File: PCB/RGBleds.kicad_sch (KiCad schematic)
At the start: 17 parts, among them Q21 Q_NPN_BCE, Q22 Q_NPN_BCE, Q23 Q_NPN_BCE

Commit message: made some Changes
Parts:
- removed R22, R24, R26: 1k, Resistor_SMD:R_1206_3216Metric_Pad1.30x1.75mm_HandSolder, symbol Device:R
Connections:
- net LEDG_VCC is gone; now on net VCC: D21.5 (GA), D22.5 (GA), D23.5 (GA), D24.5 (GA), D25.5 (GA), D26.5 (GA), D27.5 (GA), D28.5 (GA)
- net LEDR_VCC is gone; now on net VCC: D21.6 (RA), D22.6 (RA), D23.6 (RA), D24.6 (RA), D25.6 (RA), D26.6 (RA), D27.6 (RA), D28.6 (RA)
- net LEDR: now reaches Q21.1 (B)
- net LEDG: now reaches Q22.1 (B)
- net LEDB: now reaches Q23.1 (B)
- net LEDB_VCC renamed VCC

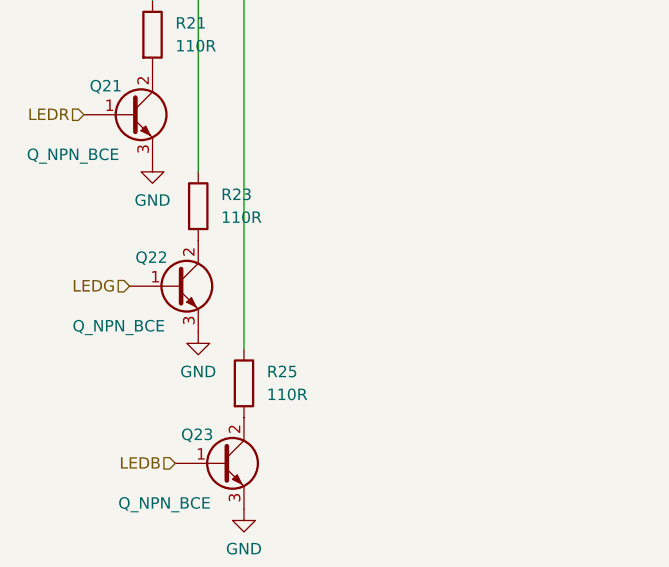
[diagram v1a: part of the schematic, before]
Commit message: added Capacitor and updated PCB
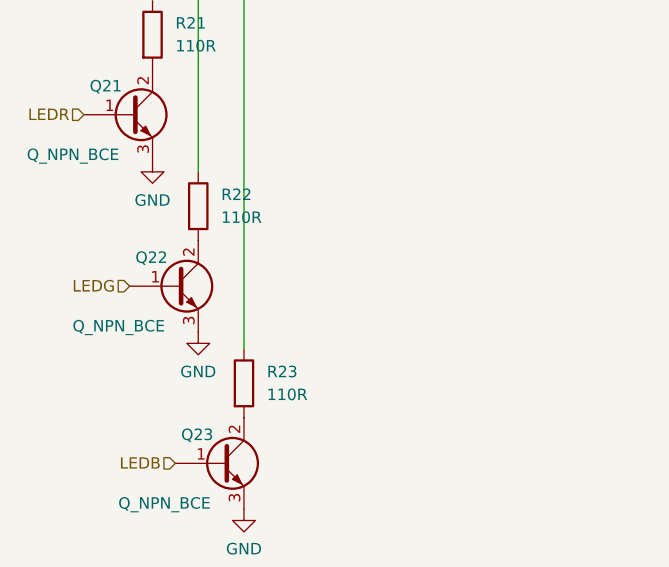
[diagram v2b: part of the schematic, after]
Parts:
- renumbered R23 to R22, R25 to R23
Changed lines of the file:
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@@
   (symbol (lib_id "power:GND") (at 81.28 128.27 0) (unit 1)
     (in_bom yes) (on_board yes) (fields_autoplaced)
-    (property "Reference" "#PWR025" (id 0) (at 81.28 134.62 0)
+    (property "Reference" "#PWR022" (id 0) (at 81.28 134.62 0)
       (effects (font (size 1.27 1.27)) hide)
     )
@@
   (symbol (lib_id "power:VCC") (at 148.59 75.565 0) (unit 1)
     (in_bom yes) (on_board yes) (fields_autoplaced)
-    (property "Reference" "#PWR?" (id 0) (at 148.59 79.375 0)
+    (property "Reference" "#PWR021" (id 0) (at 148.59 79.375 0)
       (effects (font (size 1.27 1.27)) hide)
     )
@@
   (symbol (lib_id "power:GND") (at 86.36 147.32 0) (unit 1)
     (in_bom yes) (on_board yes) (fields_autoplaced)
-    (property "Reference" "#PWR026" (id 0) (at 86.36 153.67 0)
+    (property "Reference" "#PWR023" (id 0) (at 86.36 153.67 0)
       (effects (font (size 1.27 1.27)) hide)
     )
@@
   (symbol (lib_id "power:GND") (at 91.44 167.005 0) (unit 1)
     (in_bom yes) (on_board yes) (fields_autoplaced)
-    (property "Reference" "#PWR027" (id 0) (at 91.44 173.355 0)
+    (property "Reference" "#PWR024" (id 0) (at 91.44 173.355 0)
       (effects (font (size 1.27 1.27)) hide)
     )
@@
   (symbol (lib_id "Device:R") (at 91.44 153.035 0) (unit 1)
     (in_bom yes) (on_board yes)
-    (property "Reference" "R25" (id 0) (at 93.98 151.7649 0)
+    (property "Reference" "R23" (id 0) (at 93.98 151.7649 0)
       (effects (font (size 1.27 1.27)) (justify left))
     )
@@
   (symbol (lib_id "Device:R") (at 86.36 133.35 0) (unit 1)
     (in_bom yes) (on_board yes)
-    (property "Reference" "R23" (id 0) (at 88.9 132.0799 0)
-      (effects (font (size 1.27 1.27)) (justify left))
-    )
+    (property "Reference" "R22" (id 0) (at 88.9 132.0799 0)
+      (effects (font (size 1.27 1.27)) (justify left))
+    )

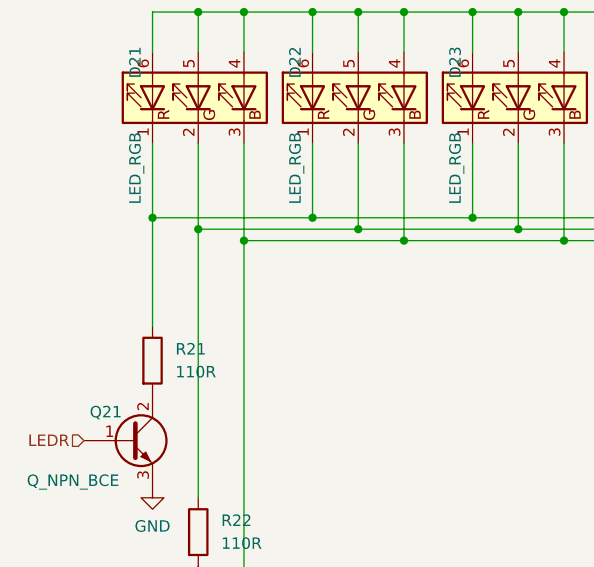
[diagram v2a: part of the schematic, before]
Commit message: made some changes on RGB LEDs
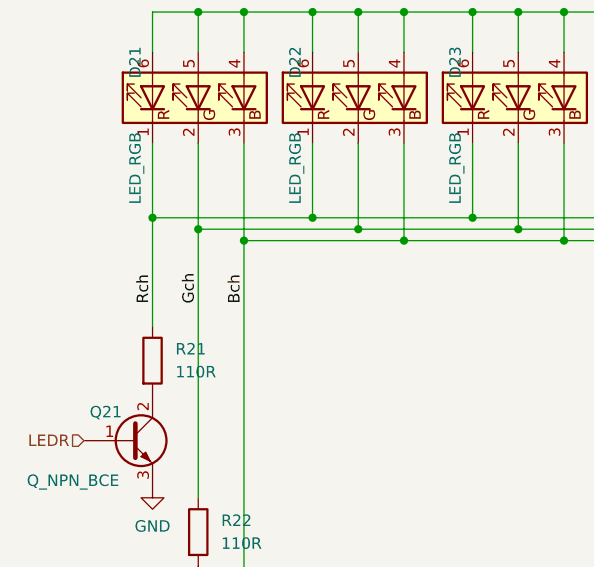
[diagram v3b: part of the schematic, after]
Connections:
- net Rch: now reaches D21.1 (RK), D22.1 (RK), D23.1 (RK), D24.1 (RK), D25.1 (RK), D26.1 (RK), D27.1 (RK), D28.1 (RK), R21.1
- net Gch: now reaches D21.2 (GK), D22.2 (GK), D23.2 (GK), D24.2 (GK), D25.2 (GK), D26.2 (GK), D27.2 (GK), D28.2 (GK), R22.1
- net Bch: now reaches D21.3 (BK), D22.3 (BK), D23.3 (BK), D24.3 (BK), D25.3 (BK), D26.3 (BK), D27.3 (BK), D28.3 (BK), R23.1
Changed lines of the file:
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@@
     (stroke (width 0) (type default) (color 0 0 0 0))
+  )
+  (label "Bch" (at 91.44 107.95 90)
+    (effects (font (size 1.27 1.27)) (justify left bottom))
+  )
+  (label "Rch" (at 81.28 107.95 90)
+    (effects (font (size 1.27 1.27)) (justify left bottom))
+  )
+  (label "Gch" (at 86.36 107.95 90)
+    (effects (font (size 1.27 1.27)) (justify left bottom))
   )
   (hierarchical_label "LEDG" (shape input) (at 78.74 142.24 180)
